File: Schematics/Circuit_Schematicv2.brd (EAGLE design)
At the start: 139.1 x 33.1 mm, 66 parts, among them Q2 LE33CZ

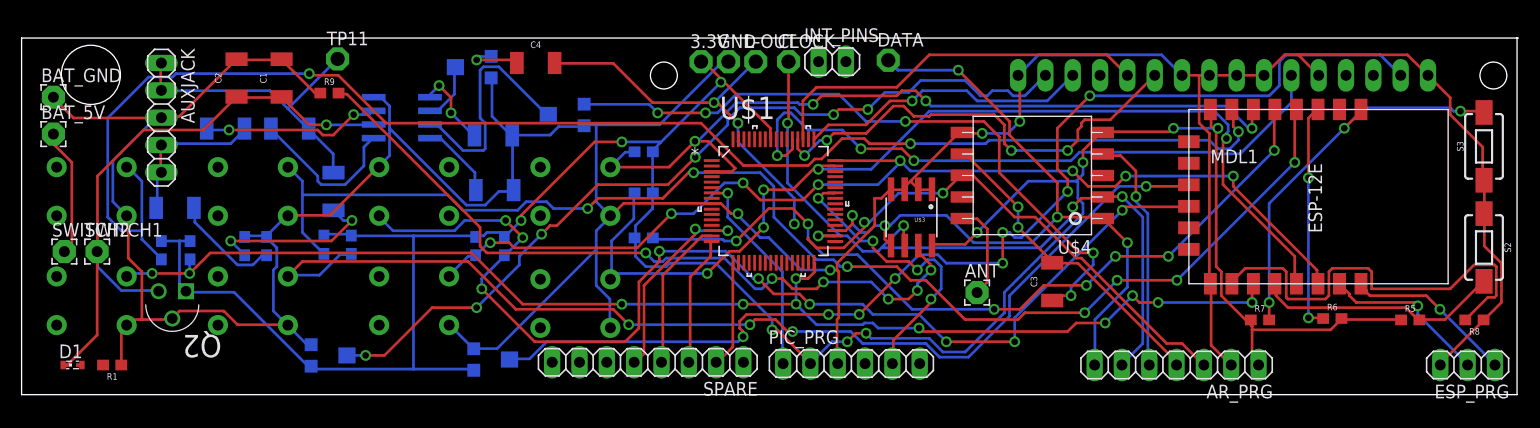
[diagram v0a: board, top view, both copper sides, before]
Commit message: Finished the PCB board and schematic
Changes might have to be made based on the testing on Friday the 10th
March
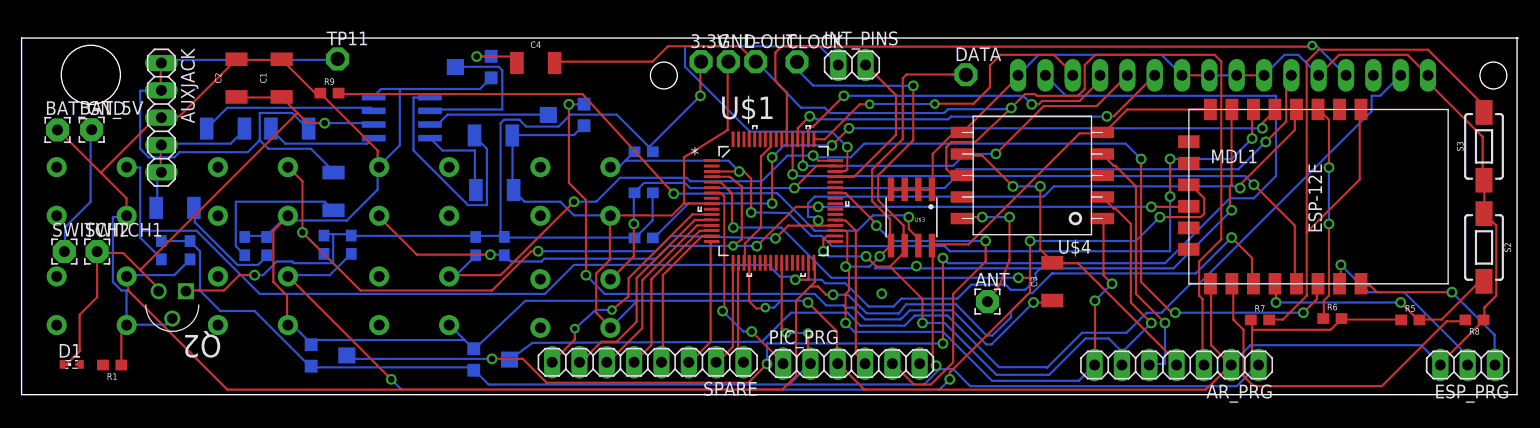
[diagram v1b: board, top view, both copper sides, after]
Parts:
- moved DATA 7.34 mm to (4.04, 47.7)
- moved BAT_5V 3.58 mm to (-77.2, 42.6)
- moved BAT_GND 3.07 mm to (-80.4, 42.5)
- moved INT_PINS 1.85 mm to (-6.55, 48.6)
- moved ANT 1.28 mm to (6.05, 26.6)
- moved CLOCK 0.79 mm to (-11.7, 48.9)
- moved D1 0.09 mm to (-79.1, 20.8)
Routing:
- net RS: track 0.00 -> 64.5 mm, vias 0 -> 1
- net A: track 78.6 -> 131.2 mm, vias 6 -> 4
- net GND: track 364.0 -> 405.8 mm, vias 4 -> 2
- net MUTE: track 103.0 -> 144.7 mm, vias 4 -> 6
- net INT2: track 0.00 -> 38.3 mm, vias 0 -> 1
- net 3.3V: track 247.2 -> 279.1 mm, vias 10 -> 5
- net DB6: track 0.00 -> 31.1 mm, vias 0 -> 2
- net L-OUT: track 84.1 -> 109.9 mm, vias 5 -> 1
- net OUT_1: track 29.3 -> 54.5 mm
- net REST: track 37.1 -> 59.5 mm, vias 3 -> 0
- net RF7: track 0.00 -> 22.0 mm, vias 0 -> 2
- net RF6: track 0.00 -> 20.3 mm
- net FAV3: track 118.7 -> 136.9 mm, vias 11 -> 2
- net RF5: track 0.00 -> 17.7 mm
- net PREVIOUS: track 105.7 -> 88.3 mm, vias 9 -> 5
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
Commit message: finished the PCB
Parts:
- D1: value (none) -> BLUE; device adafruit:SMARTLED-TTW -> SparkFun-LED:LED-1206
- moved R1 2.72 mm to (-72.6, 20.8), turned to 270 degrees
- moved D1 1.75 mm to (-77.6, 19.8), turned to 0 degrees
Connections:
- net N$18: now also D1.C; no longer D1.C@1
- net VDD: now also D1.A; no longer D1.A@1
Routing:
- net FAV2: track 149.6 -> 133.7 mm
- net N$18: track 0.00 -> 3.88 mm
- net DATA: track 79.5 -> 80.4 mm
- net PREVIOUS: track 88.3 -> 89.2 mm
- net N$1: track 12.5 -> 13.2 mm
- net VDD: track 53.6 -> 54.3 mm
- added copper zone on layer 16, net N$4
- added copper zone on layer 1, net N$5
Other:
- outline, holes or cut-outs redrawn
- board text added: "+"
- board text added: "-"
- board text added: "GROUP 14 FM PROJECT"
- board text added: "OUT_1"

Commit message: Final changes to make ESP work
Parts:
- added R18: 300, SparkFun-Resistors:0603
- added S1: GPIO0 ESP, SparkFun-Switches:TACTILE_SWITCH_SMD_6.0X3.5MM
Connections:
- removed net N$8: MDL1.12, R5.2, S2.2
- net ENABLE: now also R18.2; no longer MDL1.5
- net GND: now also S1.1
- net MUTE: now also MDL1.5, R18.1, S1.2; no longer MDL1.19
- net PREVIOUS: now also MDL1.12, R5.2, S2.2; no longer MDL1.20
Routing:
- net N$8: track 23.2 -> 0.00 mm, vias 2 -> 0
- net PREVIOUS: track 89.2 -> 112.4 mm, vias 5 -> 7
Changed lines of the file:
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@@
 <?xml version="1.0" encoding="utf-8"?>
 <!DOCTYPE eagle SYSTEM "eagle.dtd">
-<eagle version="8.0.2">
+<eagle version="8.0.0">
 <drawing>
 <settings>
@@
 <attribute name="PROD_ID" value="RES-12428" x="-41.91" y="48.387" size="1.778" layer="28" font="vector" rot="MR270" display="off"/>
 </element>
+<element name="R18" library="SparkFun-Resistors" package="0603" value="300" x="-89.154" y="8.509">
+<attribute name="PROD_ID" value="RES-08269" x="-89.154" y="8.509" size="1.778" layer="27" display="off"/>
+</element>
+<element name="S1" library="SparkFun-Switches" package="TACTILE_SWITCH_SMD_6.0X3.5MM" value="GPIO0 ESP" x="-84.8614" y="4.1148">
+<attribute name="SF_SKU" value="COM-08229" x="-84.8614" y="4.1148" size="1.778" layer="27" display="off"/>
+<attribute name="PROD_ID" value="SWCH-00815" x="-84.8614" y="4.1148" size="1.778" layer="27" display="off"/>
+</element>
 </elements>
 <signals>
@@
 <wire x1="-14.4018" y1="26.035" x2="-14.605" y2="25.8318" width="0.2032" layer="16"/>
 <wire x1="-14.605" y1="25.8318" x2="-14.732" y2="25.9588" width="0.2032" layer="1"/>
+<contactref element="S1" pad="1"/>
+<wire x1="-72.5932" y1="21.6526" x2="-88.0114" y2="4.1148" width="0" layer="19" extent="1-1"/>
 </signal>
 <signal name="N$11">
@@
 <contactref element="S8" pad="1"/>
 <contactref element="R11" pad="1"/>
-<contactref element="MDL1" pad="20"/>
 <wire x1="-40.16375" y1="30.95625" x2="-38.89375" y2="30.95625" width="0.2032" layer="16"/>
 <wire x1="-46.99" y1="30.95625" x2="-40.16375" y2="30.95625" width="0.2032" layer="1"/>
@@
 <wire x1="-35.40125" y1="30.32125" x2="-38.25875" y2="30.32125" width="0.2032" layer="16"/>
 <wire x1="-38.735" y1="30.7975" x2="-38.25875" y2="30.32125" width="0.2032" layer="16"/>
-<wire x1="24.765" y1="35.40125" x2="24.765" y2="35.45" width="0.2032" layer="1"/>
 <wire x1="-38.735" y1="30.7975" x2="-38.862" y2="30.9" width="0.2032" layer="16"/>
 <via x="-40.16375" y="30.95625" extent="1-16" drill="0.6096"/>
@@
 <wire x1="-16.9672" y1="32.4104" x2="-16.9672" y2="32.2834" width="0.2032" layer="1"/>
 <wire x1="-16.9672" y1="32.2834" x2="-17.526" y2="31.7246" width="0.2032" layer="1"/>
+<contactref element="MDL1" pad="12"/>
+<contactref element="R5" pad="2"/>
+<contactref element="S2" pad="2"/>
+<wire x1="48.26" y1="24.92375" x2="46.19625" y2="24.92375" width="0.2032" layer="1"/>
+<wire x1="51.7525" y1="28.41625" x2="48.26" y2="24.92375" width="0.2032" layer="1"/>
+<wire x1="52.07" y1="28.41625" x2="51.7525" y2="28.41625" width="0.2032" layer="1"/>
+<wire x1="46.19625" y1="24.92375" x2="46.189" y2="24.892" width="0.2032" layer="1"/>
+<wire x1="52.07" y1="28.41625" x2="52.197" y2="28.473" width="0.2032" layer="1"/>
+<wire x1="32.86125" y1="26.51125" x2="32.86125" y2="28.09875" width="0.2032" layer="1"/>
+<wire x1="44.45" y1="26.51125" x2="32.86125" y2="26.51125" width="0.2032" layer="16"/>
+<wire x1="46.0375" y1="24.92375" x2="44.45" y2="26.51125" width="0.2032" layer="1"/>
+<wire x1="32.86125" y1="28.09875" x2="32.765" y2="28.25" width="0.2032" layer="1"/>
+<wire x1="46.0375" y1="24.92375" x2="46.189" y2="24.892" width="0.2032" layer="1"/>
+<via x="32.86125" y="26.51125" extent="1-16" drill="0.6096"/>
+<via x="44.45" y="26.51125" extent="1-16" drill="0.6096"/>
+<wire x1="24.765" y1="35.40125" x2="32.765" y2="28.25" width="0" layer="19" extent="1-1"/>
 </signal>
 <signal name="MUTE">
@@
 <contactref element="S11" pad="1"/>
 <contactref element="R14" pad="2"/>
-<contactref element="MDL1" pad="19"/>
 <wire x1="-55.08625" y1="29.05125" x2="-53.18125" y2="30.95625" width="0.2032" layer="16"/>
 <wire x1="-58.89625" y1="29.05125" x2="-55.08625" y2="29.05125" width="0.2032" layer="16"/>
@@
 <wire x1="-49.37125" y1="19.3675" x2="-48.41875" y2="18.415" width="0.2032" layer="16"/>
 <wire x1="-58.89625" y1="28.8925" x2="-49.37125" y2="19.3675" width="0.2032" layer="1"/>
-<wire x1="24.765" y1="37.30625" x2="24.765" y2="37.45" width="0.2032" layer="1"/>
 <wire x1="-58.89625" y1="28.8925" x2="-58.9788" y2="28.9306" width="0.2032" layer="1"/>
 <via x="22.06625" y="34.44875" extent="1-16" drill="0.6096"/>
@@
 <wire x1="10.00125" y1="28.8544" x2="9.95045" y2="28.8036" width="0.2032" layer="1"/>
 <wire x1="-8.4582" y1="28.8036" x2="8.9154" y2="28.8036" width="0.2032" layer="16"/>
+<contactref element="MDL1" pad="5"/>
+<contactref element="S1" pad="2"/>
+<contactref element="R18" pad="1"/>
+<wire x1="-81.7114" y1="4.1148" x2="-90.004" y2="8.509" width="0" layer="19" extent="1-1"/>
+<wire x1="-58.9788" y1="28.9306" x2="-81.7114" y2="4.1148" width="0" layer="19" extent="1-16"/>
+<wire x1="32.765" y1="44.45" x2="25.0825" y2="37.30625" width="0" layer="19" extent="1-1"/>
 </signal>
 <signal name="VOLUP">
@@
 <signal name="ENABLE">
 <contactref element="R15" pad="2"/>
-<contactref element="MDL1" pad="5"/>
 <wire x1="-21.74875" y1="35.71875" x2="-24.92375" y2="32.54375" width="0.2032" layer="16"/>
 <wire x1="-13.97" y1="35.71875" x2="-21.74875" y2="35.71875" width="0.2032" layer="16"/>
@@
 <wire x1="32.86125" y1="44.45" x2="31.59125" y2="43.18" width="0.2032" layer="1"/>
 <wire x1="-24.92375" y1="32.54375" x2="-25.058" y2="32.512" width="0.2032" layer="16"/>
-<wire x1="32.86125" y1="44.45" x2="32.765" y2="44.45" width="0.2032" layer="1"/>
 <via x="-13.97" y="35.71875" extent="1-16" drill="0.6096"/>
 <via x="-13.5382" y="39.8018" extent="1-16" drill="0.6096"/>
@@
 <wire x1="-13.5382" y1="39.8018" x2="-13.5382" y2="36.15055" width="0.2032" layer="1"/>
 <wire x1="-13.5382" y1="36.15055" x2="-13.97" y2="35.71875" width="0.2032" layer="1"/>
-</signal>
-<signal name="N$8">
-<contactref element="MDL1" pad="12"/>
-<contactref element="R5" pad="2"/>
-<contactref element="S2" pad="2"/>
-<wire x1="48.26" y1="24.92375" x2="46.19625" y2="24.92375" width="0.2032" layer="1"/>
-<wire x1="51.7525" y1="28.41625" x2="48.26" y2="24.92375" width="0.2032" layer="1"/>
-<wire x1="52.07" y1="28.41625" x2="51.7525" y2="28.41625" width="0.2032" layer="1"/>
-<wire x1="46.19625" y1="24.92375" x2="46.189" y2="24.892" width="0.2032" layer="1"/>
-<wire x1="52.07" y1="28.41625" x2="52.197" y2="28.473" width="0.2032" layer="1"/>
-<wire x1="32.86125" y1="26.51125" x2="32.86125" y2="28.09875" width="0.2032" layer="1"/>
-<wire x1="44.45" y1="26.51125" x2="32.86125" y2="26.51125" width="0.2032" layer="16"/>
-<wire x1="46.0375" y1="24.92375" x2="44.45" y2="26.51125" width="0.2032" layer="1"/>
-<wire x1="32.86125" y1="28.09875" x2="32.765" y2="28.25" width="0.2032" layer="1"/>
-<wire x1="46.0375" y1="24.92375" x2="46.189" y2="24.892" width="0.2032" layer="1"/>
-<via x="32.86125" y="26.51125" extent="1-16" drill="0.6096"/>
-<via x="44.45" y="26.51125" extent="1-16" drill="0.6096"/>
+<contactref element="R18" pad="2"/>
+<wire x1="-25.058" y1="32.512" x2="-88.304" y2="8.509" width="0" layer="19" extent="1-16"/>
 </signal>
 <signal name="DB4">

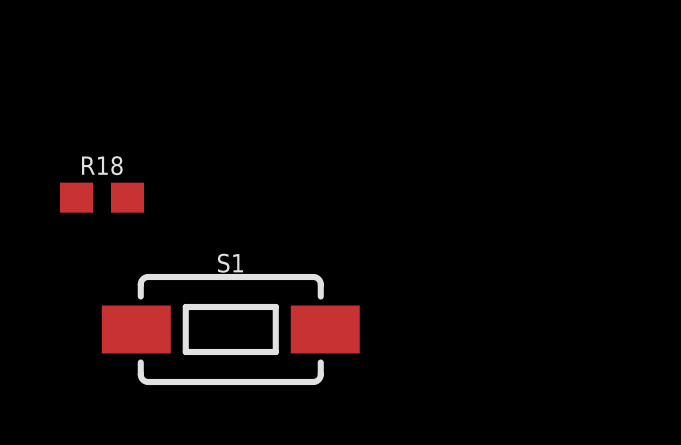
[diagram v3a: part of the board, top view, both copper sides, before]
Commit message: Removed unnecessary switch that I put in on GPIO14
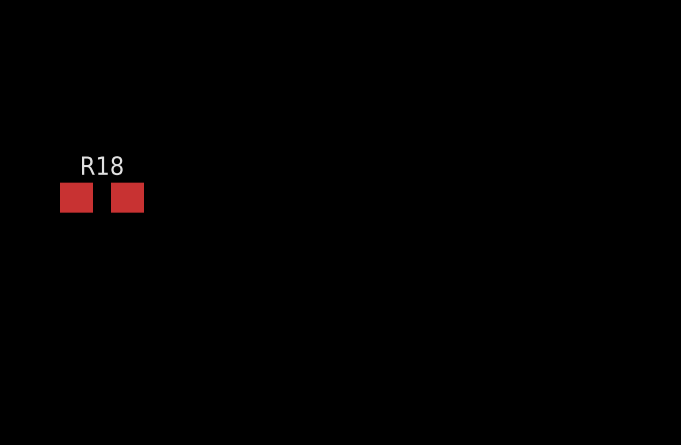
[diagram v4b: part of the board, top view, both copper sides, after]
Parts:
- removed S1: GPIO0 ESP, SparkFun-Switches:TACTILE_SWITCH_SMD_6.0X3.5MM
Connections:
- net GND: no longer S1.1
- net MUTE: no longer S1.2
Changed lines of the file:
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@@
 <attribute name="PROD_ID" value="RES-08269" x="-89.154" y="8.509" size="1.778" layer="27" display="off"/>
-</element>
-<element name="S1" library="SparkFun-Switches" package="TACTILE_SWITCH_SMD_6.0X3.5MM" value="GPIO0 ESP" x="-84.8614" y="4.1148">
-<attribute name="SF_SKU" value="COM-08229" x="-84.8614" y="4.1148" size="1.778" layer="27" display="off"/>
-<attribute name="PROD_ID" value="SWCH-00815" x="-84.8614" y="4.1148" size="1.778" layer="27" display="off"/>
 </element>
 </elements>
@@
 <wire x1="-14.4018" y1="26.035" x2="-14.605" y2="25.8318" width="0.2032" layer="16"/>
 <wire x1="-14.605" y1="25.8318" x2="-14.732" y2="25.9588" width="0.2032" layer="1"/>
-<contactref element="S1" pad="1"/>
-<wire x1="-72.5932" y1="21.6526" x2="-88.0114" y2="4.1148" width="0" layer="19" extent="1-1"/>
 </signal>
 <signal name="N$11">
@@
 <wire x1="-8.4582" y1="28.8036" x2="8.9154" y2="28.8036" width="0.2032" layer="16"/>
 <contactref element="MDL1" pad="5"/>
-<contactref element="S1" pad="2"/>
 <contactref element="R18" pad="1"/>
-<wire x1="-81.7114" y1="4.1148" x2="-90.004" y2="8.509" width="0" layer="19" extent="1-1"/>
-<wire x1="-58.9788" y1="28.9306" x2="-81.7114" y2="4.1148" width="0" layer="19" extent="1-16"/>
+<wire x1="-58.9788" y1="28.9306" x2="-90.004" y2="8.509" width="0" layer="19" extent="1-16"/>
 <wire x1="32.765" y1="44.45" x2="25.0825" y2="37.30625" width="0" layer="19" extent="1-1"/>
 </signal>

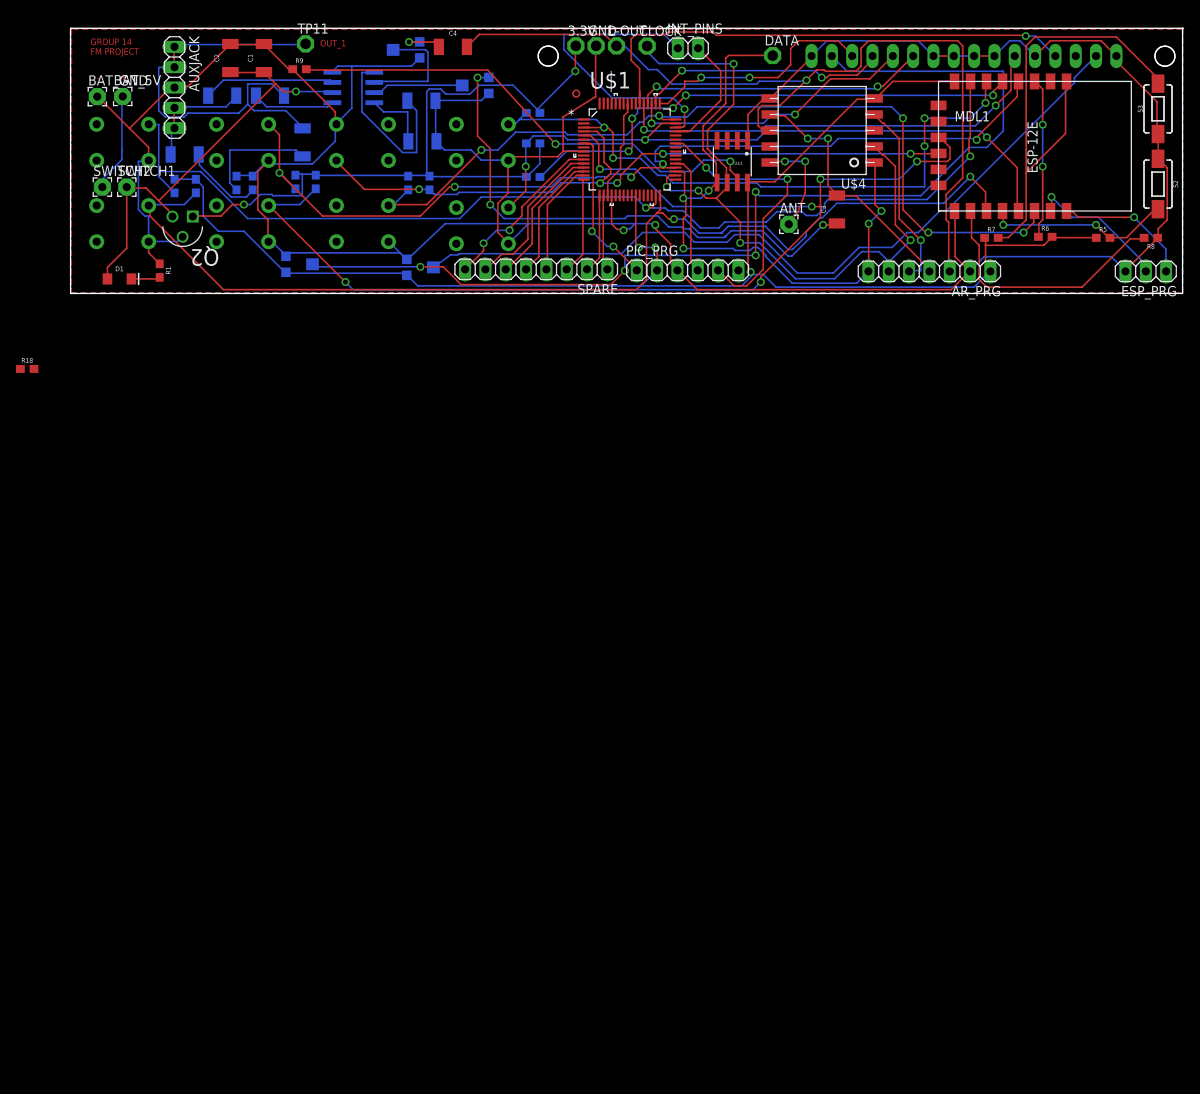
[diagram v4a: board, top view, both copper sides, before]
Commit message: Modified circuit to include transistors
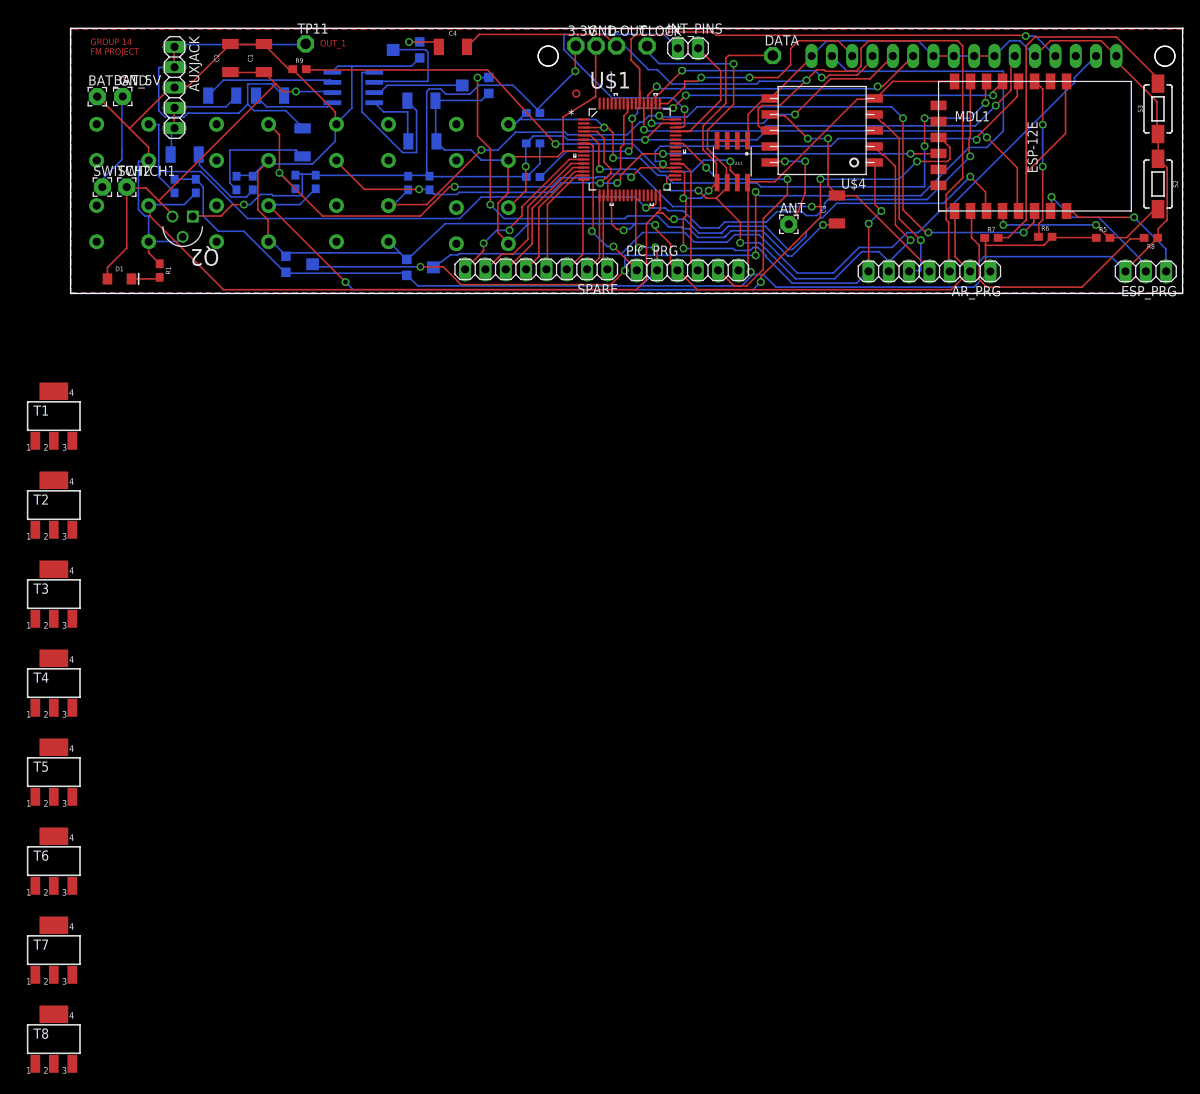
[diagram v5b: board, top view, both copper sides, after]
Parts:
- removed R18: 300, SparkFun-Resistors:0603
- added T1, T2, T3, T4, T5, T6, T7, T8: (no value), zetex:SOT223
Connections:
- new net FAV1_GATE: MDL1.4, T6.1
- new net FAV2_GATE: MDL1.7, T7.1
- new net FAV3_GATE: MDL1.11, T8.1
- new net MUTE_GATE: MDL1.5, T5.1
- new net NEXT_GATE: MDL1.6, T1.1
- new net PREVIOUS_GATE: MDL1.12, R5.2, S2.2, T2.1
- new net VOLDOWN_GATE: MDL1.13, T4.1
- new net VOLUP_GATE: MDL1.14, T3.1
- net ENABLE: no longer R18.2
- net FAV1: now also T6.2, T6.4; no longer MDL1.4
- net FAV2: now also T7.2, T7.4; no longer MDL1.7
- net FAV3: now also T8.2, T8.4; no longer MDL1.11
- net GND: now also T1.3, T2.3, T3.3, T4.3, T5.3, T6.3, T7.3, T8.3
- net MUTE: now also T5.2, T5.4; no longer MDL1.5, R18.1
- net NEXT: now also T1.2, T1.4; no longer MDL1.6
- net PREVIOUS: now also T2.2, T2.4; no longer MDL1.12, R5.2, S2.2
- net VOLDOWN: now also T4.2, T4.4; no longer MDL1.13
- net VOLUP: now also T3.2, T3.4; no longer MDL1.14
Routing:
- net PREVIOUS_GATE: track 0.00 -> 23.2 mm, vias 0 -> 2
- net PREVIOUS: track 112.4 -> 89.1 mm, vias 7 -> 5
